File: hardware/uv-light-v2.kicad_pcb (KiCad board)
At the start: 2 copper layers, 15 x 25 mm, 24 parts, among them P1 CON-SENSOR2, P2 DEBUG, P3 BOOT, U1 XMC1XXX24, U2 VEML6075, U3 DRILL, U4 DRILL, U5 DRILL, U6 DRILL

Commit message: fix logos, fix origin
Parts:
- moved G*** 7.50 mm to (136.9, 87.9), turned to 270 degrees
- moved VAL 5.50 mm to (136.9, 82.4), turned to 270 degrees
- moved VAL 1.50 mm to (136.9, 93.9), turned to 270 degrees
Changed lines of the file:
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@@
-(kicad_pcb (version 4) (host pcbnew 4.0.7-e2-6376~58~ubuntu17.04.1)
+(kicad_pcb (version 4) (host pcbnew 4.0.7-e2-6376~61~ubuntu18.04.1)
   (general
     (links 45)
@@
     (pad_drill 0.6)
     (pad_to_mask_clearance 0)
-    (aux_axis_origin 129.4 100.4)
-    (grid_origin 129.4 100.4)
+    (aux_axis_origin 129.4 75.4)
+    (grid_origin 129.4 75.4)
     (visible_elements FFFFFF7F)
     (pcbplotparams
@@
   )
   (module kicad-libraries:CE_5mm (layer B.Cu)
-    (at 136.9 95.4 90)
-    (fp_text reference VAL (at 0 0 90) (layer B.SilkS) hide
+    (at 136.9 93.9 270)
+    (fp_text reference VAL (at 0 0 270) (layer B.SilkS) hide
       (effects (font (size 0.2 0.2) (thickness 0.05)) (justify mirror))
     )
-    (fp_text value CE_5mm (at 0 0 90) (layer B.SilkS) hide
+    (fp_text value CE_5mm (at 0 0 270) (layer B.SilkS) hide
       (effects (font (size 0.2 0.2) (thickness 0.05)) (justify mirror))
     )
@@
   )
   (module kicad-libraries:Logo_CoMCU (layer B.Cu)
-    (at 136.9 80.4 90)
-    (fp_text reference G*** (at 0 0 90) (layer B.SilkS) hide
+    (at 136.9 87.9 270)
+    (fp_text reference G*** (at 0 0 270) (layer B.SilkS) hide
       (effects (font (thickness 0.3)) (justify mirror))
     )
-    (fp_text value LOGO (at 0.75 0 90) (layer B.SilkS) hide
+    (fp_text value LOGO (at 0.75 0 270) (layer B.SilkS) hide
       (effects (font (thickness 0.3)) (justify mirror))
     )
@@
   )
   (module kicad-libraries:WEEE_7mm (layer B.Cu)
-    (at 136.9 87.9 90)
-    (fp_text reference VAL (at 0 0 90) (layer B.SilkS) hide
+    (at 136.9 82.4 270)
+    (fp_text reference VAL (at 0 0 270) (layer B.SilkS) hide
       (effects (font (size 0.2 0.2) (thickness 0.05)) (justify mirror))
     )
-    (fp_text value WEEE_7mm (at 0.75 0 90) (layer B.SilkS) hide
+    (fp_text value WEEE_7mm (at 0.75 0 270) (layer B.SilkS) hide
       (effects (font (size 0.2 0.2) (thickness 0.05)) (justify mirror))
     )
@@
     )
   )
-  (gr_text tinkerforge.com (at 141.72 87.9 270) (layer B.SilkS)
+  (gr_text tinkerforge.com (at 141.9 87.9 90) (layer B.SilkS)
     (effects (font (size 0.7 0.7) (thickness 0.15)) (justify mirror))
   )

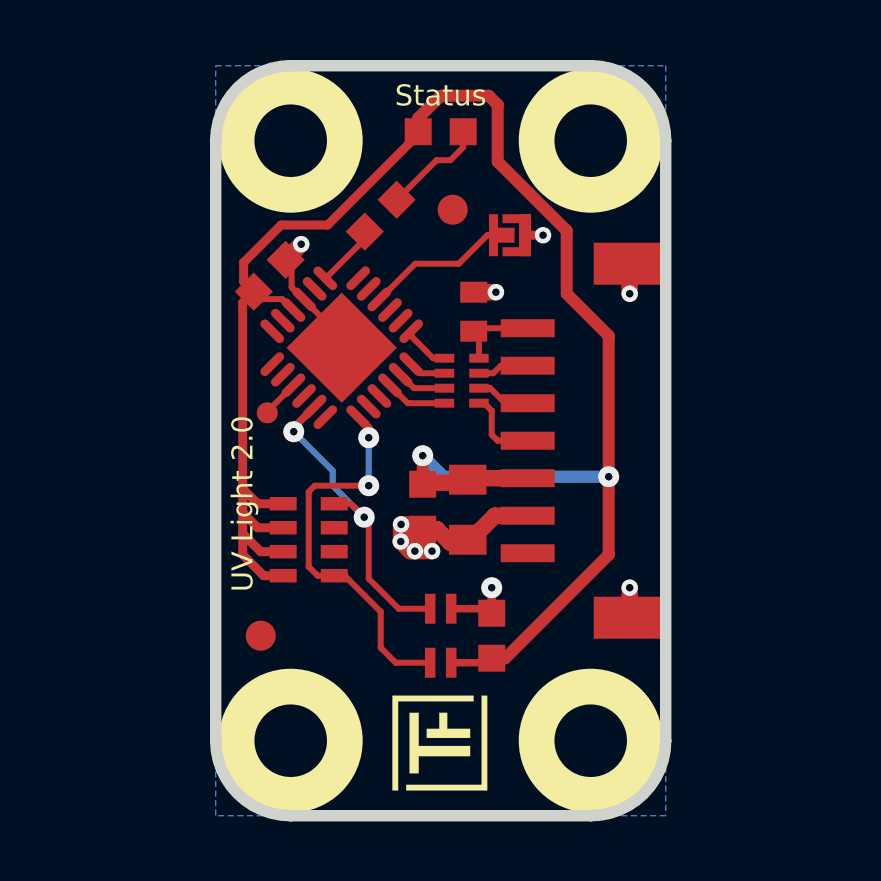
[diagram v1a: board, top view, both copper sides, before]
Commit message: Change capacitor footprint(s) to C0402F
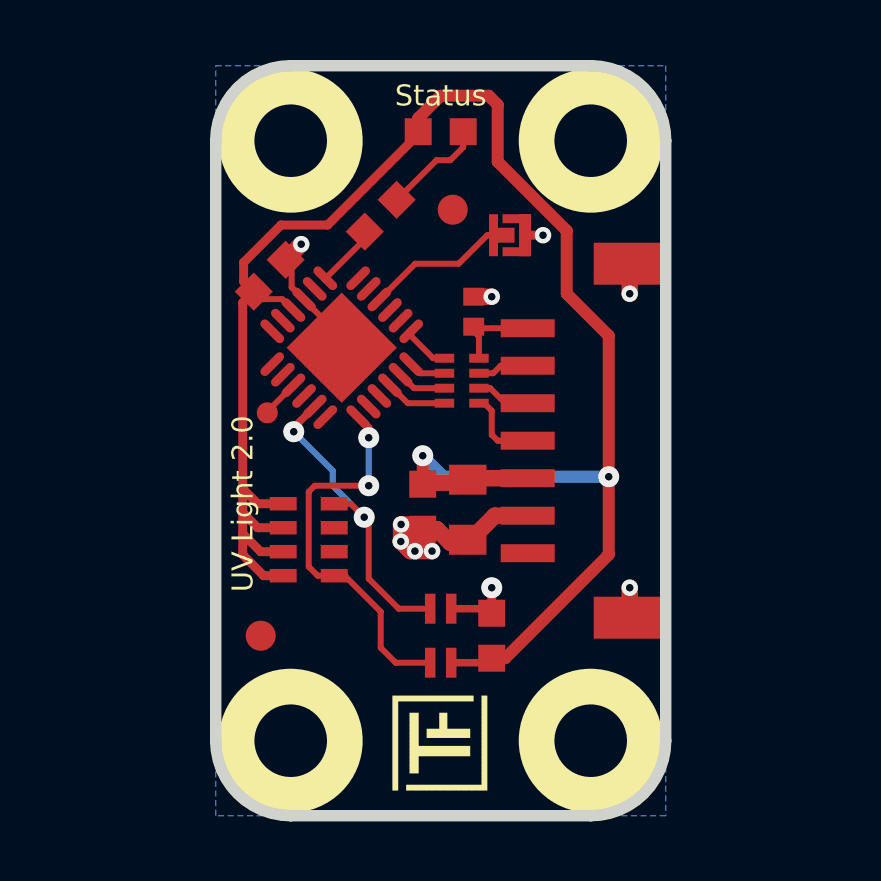
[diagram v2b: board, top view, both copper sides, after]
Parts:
- C1: footprint kicad-libraries:C0402E -> kicad-libraries:C0402F
- U2: footprint OPLGA4 -> kicad-libraries:OPLGA4
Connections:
- P1 pad 1: (no net) -> Net-(P1-Pad1)
- RP2 pad 6: (no net) -> Net-(RP2-Pad6)
- RP2 pad 7: (no net) -> Net-(RP2-Pad7)
- U1 pad 11: (no net) -> Net-(U1-Pad11)
- U1 pad 12: (no net) -> Net-(U1-Pad12)
- U1 pad 13: (no net) -> Net-(U1-Pad13)
- U1 pad 14: (no net) -> Net-(U1-Pad14)
- U1 pad 16: (no net) -> Net-(U1-Pad16)
- U1 pad 18: (no net) -> ACK
- U1 pad 2: (no net) -> Net-(U1-Pad2)
- U1 pad 20: (no net) -> Net-(U1-Pad20)
- U1 pad 21: (no net) -> Net-(U1-Pad21)
- U1 pad 3: (no net) -> Net-(U1-Pad3)
- U1 pad 5: (no net) -> Net-(U1-Pad5)
- U1 pad 6: (no net) -> Net-(U1-Pad6)
- U1 pad 8: (no net) -> Net-(U1-Pad8)
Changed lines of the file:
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@@
-(kicad_pcb (version 4) (host pcbnew 4.0.7-e2-6376~61~ubuntu18.04.1)
+(kicad_pcb (version 4) (host pcbnew 4.0.2+dfsg1-stable)
   (general
     (links 45)
     (no_connects 0)
-    (area 13.871426 74.544999 145.255001 195.075)
+    (area 129.209499 75.209499 144.590501 100.590501)
     (thickness 1.6)
     (drawings 12)
@@
     (zones 0)
     (modules 24)
-    (nets 17)
+    (nets 33)
   )
   (page A4)
@@
   )
   (setup
-    (last_trace_width 0.25)
+    (last_trace_width 0.55)
     (user_trace_width 0.2)
     (user_trace_width 0.25)
@@
   (net 15 S-CS)
   (net 16 "Net-(C1-Pad2)")
+  (net 17 "Net-(P1-Pad1)")
+  (net 18 "Net-(RP2-Pad6)")
+  (net 19 "Net-(RP2-Pad7)")
+  (net 20 "Net-(U1-Pad2)")
+  (net 21 "Net-(U1-Pad3)")
+  (net 22 "Net-(U1-Pad5)")
+  (net 23 "Net-(U1-Pad6)")
+  (net 24 "Net-(U1-Pad8)")
+  (net 25 "Net-(U1-Pad11)")
+  (net 26 "Net-(U1-Pad12)")
+  (net 27 "Net-(U1-Pad13)")
+  (net 28 "Net-(U1-Pad14)")
+  (net 29 "Net-(U1-Pad16)")
+  (net 30 ACK)
+  (net 31 "Net-(U1-Pad20)")
+  (net 32 "Net-(U1-Pad21)")
   (net_class Default "This is the default net class."
     (clearance 0.15)
@@
     (uvia_dia 0.3)
     (uvia_drill 0.1)
+    (add_net ACK)
     (add_net GND)
     (add_net "Net-(C1-Pad2)")
     (add_net "Net-(D1-Pad2)")
+    (add_net "Net-(P1-Pad1)")
     (add_net "Net-(P1-Pad4)")
     (add_net "Net-(P1-Pad5)")
@@
     (add_net "Net-(P3-Pad2)")
     (add_net "Net-(R1-Pad1)")
+    (add_net "Net-(RP2-Pad6)")
+    (add_net "Net-(RP2-Pad7)")
+    (add_net "Net-(U1-Pad11)")
+    (add_net "Net-(U1-Pad12)")
+    (add_net "Net-(U1-Pad13)")
+    (add_net "Net-(U1-Pad14)")
+    (add_net "Net-(U1-Pad16)")
+    (add_net "Net-(U1-Pad2)")
+    (add_net "Net-(U1-Pad20)")
+    (add_net "Net-(U1-Pad21)")
+    (add_net "Net-(U1-Pad3)")
+    (add_net "Net-(U1-Pad5)")
+    (add_net "Net-(U1-Pad6)")
+    (add_net "Net-(U1-Pad8)")
     (add_net S-CLK)
     (add_net S-CS)
@@
     (fp_line (start 6 -4.3) (end -6 -4.3) (layer F.Fab) (width 0.05))
     (fp_line (start -6 -4.3) (end -6 -0.25) (layer F.Fab) (width 0.05))
-    (pad 1 smd rect (at -3.75 -4.6 90) (size 0.6 1.8) (layers F.Cu F.Paste F.Mask))
+    (pad 1 smd rect (at -3.75 -4.6 90) (size 0.6 1.8) (layers F.Cu F.Paste F.Mask)
+      (net 17 "Net-(P1-Pad1)"))
     (pad 2 smd rect (at -2.5 -4.6 90) (size 0.6 1.8) (layers F.Cu F.Paste F.Mask)
       (net 1 GND))
@@
     (pad 1 smd oval (at -2.025 -1.25 225) (size 1 0.3) (layers F.Cu F.Paste F.Mask)
       (net 12 S-MISO))
-    (pad 2 smd oval (at -2.025 -0.75 225) (size 1 0.3) (layers F.Cu F.Paste F.Mask))
-    (pad 3 smd oval (at -2.025 -0.25 225) (size 1 0.3) (layers F.Cu F.Paste F.Mask))
+    (pad 2 smd oval (at -2.025 -0.75 225) (size 1 0.3) (layers F.Cu F.Paste F.Mask)
+      (net 20 "Net-(U1-Pad2)"))
+    (pad 3 smd oval (at -2.025 -0.25 225) (size 1 0.3) (layers F.Cu F.Paste F.Mask)
+      (net 21 "Net-(U1-Pad3)"))
     (pad 4 smd oval (at -2.025 0.25 225) (size 1 0.3) (layers F.Cu F.Paste F.Mask)
       (net 11 "Net-(P3-Pad2)"))
-    (pad 5 smd oval (at -2.025 0.75 225) (size 1 0.3) (layers F.Cu F.Paste F.Mask))
-    (pad 6 smd oval (at -2.025 1.25 225) (size 1 0.3) (layers F.Cu F.Paste F.Mask))
+    (pad 5 smd oval (at -2.025 0.75 225) (size 1 0.3) (layers F.Cu F.Paste F.Mask)
+      (net 22 "Net-(U1-Pad5)"))
+    (pad 6 smd oval (at -2.025 1.25 225) (size 1 0.3) (layers F.Cu F.Paste F.Mask)
+      (net 23 "Net-(U1-Pad6)"))
     (pad 7 smd oval (at -1.25 2.025 315) (size 1 0.3) (layers F.Cu F.Paste F.Mask)
       (net 6 "Net-(R1-Pad1)"))
-    (pad 8 smd oval (at -0.75 2.025 315) (size 1 0.3) (layers F.Cu F.Paste F.Mask))
+    (pad 8 smd oval (at -0.75 2.025 315) (size 1 0.3) (layers F.Cu F.Paste F.Mask)
+      (net 24 "Net-(U1-Pad8)"))
     (pad 9 smd oval (at -0.25 2.025 315) (size 1 0.3) (layers F.Cu F.Paste F.Mask)
       (net 1 GND))
     (pad 10 smd oval (at 0.25 2.025 315) (size 1 0.3) (layers F.Cu F.Paste F.Mask)
       (net 2 VCC))
-    (pad 11 smd oval (at 0.75 2.025 315) (size 1 0.3) (layers F.Cu F.Paste F.Mask))
-    (pad 12 smd oval (at 1.25 2.025 315) (size 1 0.3) (layers F.Cu F.Paste F.Mask))
-    (pad 13 smd oval (at 2.025 1.25 225) (size 1 0.3) (layers F.Cu F.Paste F.Mask))
-    (pad 14 smd oval (at 2.025 0.75 225) (size 1 0.3) (layers F.Cu F.Paste F.Mask))
+    (pad 11 smd oval (at 0.75 2.025 315) (size 1 0.3) (layers F.Cu F.Paste F.Mask)
+      (net 25 "Net-(U1-Pad11)"))
+    (pad 12 smd oval (at 1.25 2.025 315) (size 1 0.3) (layers F.Cu F.Paste F.Mask)
+      (net 26 "Net-(U1-Pad12)"))
+    (pad 13 smd oval (at 2.025 1.25 225) (size 1 0.3) (layers F.Cu F.Paste F.Mask)
+      (net 27 "Net-(U1-Pad13)"))
+    (pad 14 smd oval (at 2.025 0.75 225) (size 1 0.3) (layers F.Cu F.Paste F.Mask)
+      (net 28 "Net-(U1-Pad14)"))
     (pad 15 smd oval (at 2.025 0.25 225) (size 1 0.3) (layers F.Cu F.Paste F.Mask)
       (net 10 "Net-(P2-Pad1)"))
-    (pad 16 smd oval (at 2.025 -0.25 225) (size 1 0.3) (layers F.Cu F.Paste F.Mask))
+    (pad 16 smd oval (at 2.025 -0.25 225) (size 1 0.3) (layers F.Cu F.Paste F.Mask)
+      (net 29 "Net-(U1-Pad16)"))
     (pad 17 smd oval (at 2.025 -0.75 225) (size 1 0.3) (layers F.Cu F.Paste F.Mask)
       (net 4 SDA))
-    (pad 18 smd oval (at 2.025 -1.25 225) (size 1 0.3) (layers F.Cu F.Paste F.Mask))
+    (pad 18 smd oval (at 2.025 -1.25 225) (size 1 0.3) (layers F.Cu F.Paste F.Mask)
+      (net 30 ACK))
     (pad 19 smd oval (at 1.25 -2.025 315) (size 1 0.3) (layers F.Cu F.Paste F.Mask)
       (net 3 SCL))
-    (pad 20 smd oval (at 0.75 -2.025 315) (size 1 0.3) (layers F.Cu F.Paste F.Mask))
-    (pad 21 smd oval (at 0.25 -2.025 315) (size 1 0.3) (layers F.Cu F.Paste F.Mask))
+    (pad 20 smd oval (at 0.75 -2.025 315) (size 1 0.3) (layers F.Cu F.Paste F.Mask)
+      (net 31 "Net-(U1-Pad20)"))
+    (pad 21 smd oval (at 0.25 -2.025 315) (size 1 0.3) (layers F.Cu F.Paste F.Mask)
+      (net 32 "Net-(U1-Pad21)"))
     (pad 22 smd oval (at -0.25 -2.025 315) (size 1 0.3) (layers F.Cu F.Paste F.Mask)
       (net 15 S-CS))
@@
       (xy 2.48217 3.513666) (xy 2.482863 3.409859) (xy 2.482863 3.409859)) (layer B.SilkS) (width 0.1))
   )
-  (module kicad-libraries:C0402E (layer F.Cu)
-    (at 138 83.6 270)
-    (attr smd)
-    (fp_text reference C1 (at 0 0.125 270) (layer F.Fab)
-      (effects (font (size 0.2 0.2) (thickness 0.05)))
-    )
-    (fp_text value 220pF (at 0 -0.275 270) (layer F.Fab)
-      (effects (font (size 0.2 0.2) (thickness 0.05)))
-    )
-    (fp_line (start -0.8509 -0.44958) (end 0.8509 -0.44958) (layer F.Fab) (width 0.001))
-    (fp_line (start 0.8509 -0.44958) (end 0.8509 0.44958) (layer F.Fab) (width 0.001))
-    (fp_line (start 0.8509 0.44958) (end -0.8509 0.44958) (layer F.Fab) (width 0.001))
-    (fp_line (start -0.8509 0.44958) (end -0.8509 -0.44958) (layer F.Fab) (width 0.001))
-    (pad 1 smd rect (at -0.65 0 270) (size 0.7 0.9) (layers F.Cu F.Paste F.Mask)
-      (net 1 GND))
-    (pad 2 smd rect (at 0.65 0 270) (size 0.7 0.9) (layers F.Cu F.Paste F.Mask)
-      (net 16 "Net-(C1-Pad2)"))
-    (model Capacitors_SMD/C_0402.wrl
-      (at (xyz 0 0 0))
-      (scale (xyz 1 1 1))
-      (rotate (xyz 0 0 0))
-    )
-  )
   (module kicad-libraries:C0805 (layer F.Cu)
     (at 137.8 90.2 90)
@@
     (pad 5 smd rect (at -1.19888 0.8509 90) (size 0.44958 0.89916) (layers F.Cu F.Paste F.Mask)
       (net 3 SCL))
-    (pad 6 smd rect (at -0.39878 0.8509 90) (size 0.44958 0.89916) (layers F.Cu F.Paste F.Mask))
-    (pad 7 smd rect (at 0.39878 0.8509 90) (size 0.44958 0.89916) (layers F.Cu F.Paste F.Mask))
+    (pad 6 smd rect (at -0.39878 0.8509 90) (size 0.44958 0.89916) (layers F.Cu F.Paste F.Mask)
+      (net 18 "Net-(RP2-Pad6)"))
+    (pad 7 smd rect (at 0.39878 0.8509 90) (size 0.44958 0.89916) (layers F.Cu F.Paste F.Mask)
+      (net 19 "Net-(RP2-Pad7)"))
     (pad 8 smd rect (at 1.19888 0.8509 90) (size 0.44958 0.89916) (layers F.Cu F.Paste F.Mask)
       (net 4 SDA))
@@
     )
   )
-  (module OPLGA4 (layer F.Cu)
+  (module kicad-libraries:C0402F (layer F.Cu)
+    (at 138 83.6 270)
+    (fp_text reference C1 (at 0.1 0.15 270) (layer F.Fab)
+      (effects (font (size 0.2 0.2) (thickness 0.05)))
+    )
+    (fp_text value 220pF (at 0 -0.15 270) (layer F.Fab)
+      (effects (font (size 0.2 0.2) (thickness 0.05)))
+    )
+    (fp_line (start -0.9 -0.45) (end 0.9 -0.45) (layer F.Fab) (width 0.025))
+    (fp_line (start 0.9 -0.45) (end 0.9 0.45) (layer F.Fab) (width 0.025))
+    (fp_line (start 0.9 0.45) (end -0.9 0.45) (layer F.Fab) (width 0.025))
+    (fp_line (start -0.9 0.45) (end -0.9 -0.45) (layer F.Fab) (width 0.025))
+    (pad 2 smd rect (at 0.5 0 270) (size 0.6 0.7) (layers F.Cu F.Paste F.Mask)
+      (net 16 "Net-(C1-Pad2)"))
+    (pad 1 smd rect (at -0.5 0 270) (size 0.6 0.7) (layers F.Cu F.Paste F.Mask)
+      (net 1 GND))
+    (model Capacitors_SMD/C_0402.wrl
+      (at (xyz 0 0 0))
+      (scale (xyz 1 1 1))
+      (rotate (xyz 0 0 0))
+    )
+  )
+  (module kicad-libraries:OPLGA4 (layer F.Cu)
     (at 136.9 94.4 270)
     (fp_text reference U2 (at 0 0.5 270) (layer F.Fab)
@@
     (effects (font (size 0.7 0.7) (thickness 0.15)))
   )
+  (segment (start 138 83.1) (end 138.6 83.1) (width 0.55) (layer F.Cu) (net 1))
+  (via (at 138.6 83.1) (size 0.55) (drill 0.25) (layers F.Cu B.Cu) (net 1))
   (segment (start 138.6 93.65) (end 138.6 92.8) (width 0.3) (layer F.Cu) (net 1))
   (via (at 138.6 92.8) (size 0.7) (drill 0.25) (layers F.Cu B.Cu) (net 1))
@@
   (segment (start 143.2 82) (end 143.2 83) (width 0.55) (layer F.Cu) (net 1))
   (via (at 143.2 83) (size 0.55) (drill 0.25) (layers F.Cu B.Cu) (net 1))
-  (segment (start 138 82.95) (end 138.74 82.95) (width 0.55) (layer F.Cu) (net 1))
-  (via (at 138.74 82.95) (size 0.55) (drill 0.25) (layers F.Cu B.Cu) (net 1))
   (segment (start 131.73033 81.86967) (end 132.25 81.35) (width 0.55) (layer F.Cu) (net 1))
   (via (at 132.25 81.35) (size 0.55) (drill 0.25) (layers F.Cu B.Cu) (net 1))

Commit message: specify processor
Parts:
- U1: value XMC1XXX24 -> XMC11XX24
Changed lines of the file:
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@@
-(kicad_pcb (version 4) (host pcbnew 4.0.2+dfsg1-stable)
+(kicad_pcb (version 4) (host pcbnew 4.0.7-e2-6376~61~ubuntu18.04.1)
   (general
     (links 45)
     (no_connects 0)
-    (area 129.209499 75.209499 144.590501 100.590501)
+    (area 13.871426 74.544999 145.255001 195.075)
     (thickness 1.6)
     (drawings 12)
@@
   )
   (setup
-    (last_trace_width 0.55)
+    (last_trace_width 0.25)
     (user_trace_width 0.2)
     (user_trace_width 0.25)
@@
       (effects (font (size 0.3 0.3) (thickness 0.075)))
     )
-    (fp_text value XMC1XXX24 (at 0 0.8 225) (layer F.Fab)
+    (fp_text value XMC11XX24 (at 0 0.8 225) (layer F.Fab)
       (effects (font (size 0.3 0.3) (thickness 0.075)))
     )

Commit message: specify processor
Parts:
- U1: value XMC11XX24 -> XMC1100

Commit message: Data Cleanup
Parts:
- moved G*** 16.6 mm to (148.6, 89.5), turned to 180 degrees
- moved U3 15.8 mm to (126.9, 82.9), turned to 180 degrees
- moved U4 15.8 mm to (146.9, 92.9), turned to 180 degrees
- moved U5 15.8 mm to (146.9, 82.9), turned to 180 degrees
- moved U6 15.8 mm to (126.9, 92.9), turned to 180 degrees
- moved D1 14.6 mm to (126.6, 87.9), turned to 90 degrees
- moved Fiducial_Mark 12.5 mm to (143.4, 93.9), turned to 90 degrees
- moved C4 11.2 mm to (131.4, 93.6), turned to -45 degrees
- moved R1 11.0 mm to (129.4, 89.9), turned to 135 degrees
- moved Fiducial_Mark 10.9 mm to (129.2, 87.5), turned to 90 degrees
- moved P1 10.6 mm to (136.9, 80.4), turned to 180 degrees
- moved P3 9.71 mm to (130.8, 85.9), turned to -90 degrees
- moved C5 9.50 mm to (143.4, 86.2), turned to 0 degrees
- moved U2 9.19 mm to (143.4, 87.9), turned to 0 degrees
- moved VAL 8.49 mm to (142.9, 87.9), turned to 0 degrees
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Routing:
- net GND: track 25.3 -> 23.8 mm
- net Net-(P3-Pad2): track 5.20 -> 4.17 mm
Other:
- board size 15 x 25 mm -> 25 x 15 mm
- net class Default removed
- board text added: "Copyright Tinkerforge GmbH 2023. This documentation describes Open Hardware and is licensed under the CERN OHL v. 1.1. You may redistribute and modify this documentation under the terms of the CERN OHL v.1.1. (http://ohwr.org/cernohl). This documentation is distributed WITHOUT ANY EXPRESS OR IMPLIED WARRANTY, INCLUDING OF MERCHANTABILITY, SATISFACTORY QUALITY AND FITNESS FOR A PARTICULAR PURPOSE.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"
- board text removed: "Copyright Tinkerforge GmbH 2018. This documentation describes Open Hardware and is licensed under the CERN OHL v. 1.1. You may redistribute and modify this documentation under the terms of the CERN OHL v.1.1. (http://ohwr.org/cernohl). This documentation is distributed WITHOUT ANY EXPRESS OR IMPLIED WARRANTY, INCLUDING OF MERCHANTABILITY, SATISFACTORY QUALITY AND FITNESS FOR A PARTICULAR PURPOSE.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"
